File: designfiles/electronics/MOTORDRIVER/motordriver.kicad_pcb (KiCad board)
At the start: 4 copper layers, 413 parts, among them IC1 LM5109BSDX_NOPB, IC10 LM5109BSDX_NOPB, IC11 LM5109BSDX_NOPB, IC12 LM5109BSDX_NOPB, IC13 INA2181A2IDGSR, IC14 LM5109BSDX_NOPB, IC15 LM5109BSDX_NOPB, IC16 LM5109BSDX_NOPB, IC17 LM5109BSDX_NOPB, IC18 INA2181A2IDGSR, IC2 LM5109BSDX_NOPB, IC3 LM5109BSDX_NOPB, IC4 LM5109BSDX_NOPB, IC5 INA2181A2IDGSR, IC6 BQ24133RGYR, IC7 LM5176PWPR, IC8 ATSAME53J18A-MF, IC9 LM5109BSDX_NOPB, J1 IMU1, J2 IMU2, J3 Conn_01x04_Socket, J4 Screw_Terminal_01x02, J5 1-84952-1, J6 1-84952-1, J7 1-84952-1, P1 USB_C_Plug_USB2.0, Q1 30V 71A, Q10 40V 70A, Q11 30V 71A, Q12 30V 71A, Q13 30V 71A, Q14 30V 71A, Q15 30V 71A, Q16 30V 71A, Q17 30V 71A, Q18 30V 71A, Q19 30V 71A, Q2 30V 71A, Q20 30V 71A, Q21 30V 71A, Q22 30V 71A, Q23 30V 71A, Q24 30V 71A, Q25 30V 71A, Q26 30V 71A, Q27 30V 71A, Q28 30V 71A, Q3 30V 71A, Q4 30V 71A, Q5 30V 71A, Q6 30V 71A, Q7 30V 71A, Q8 30V 71A, Q9 30V 71A, SW1 SW_DPST_x2, U1 LD1117S25TR_SOT223, U2 LD1117S33TR_SOT223, U3 LD1117S50TR_SOT223, U4 TMC4671-LA, U5 ATSAMD11D14A-M, U6 TMC4671-LA, U7 TMC4671-LA

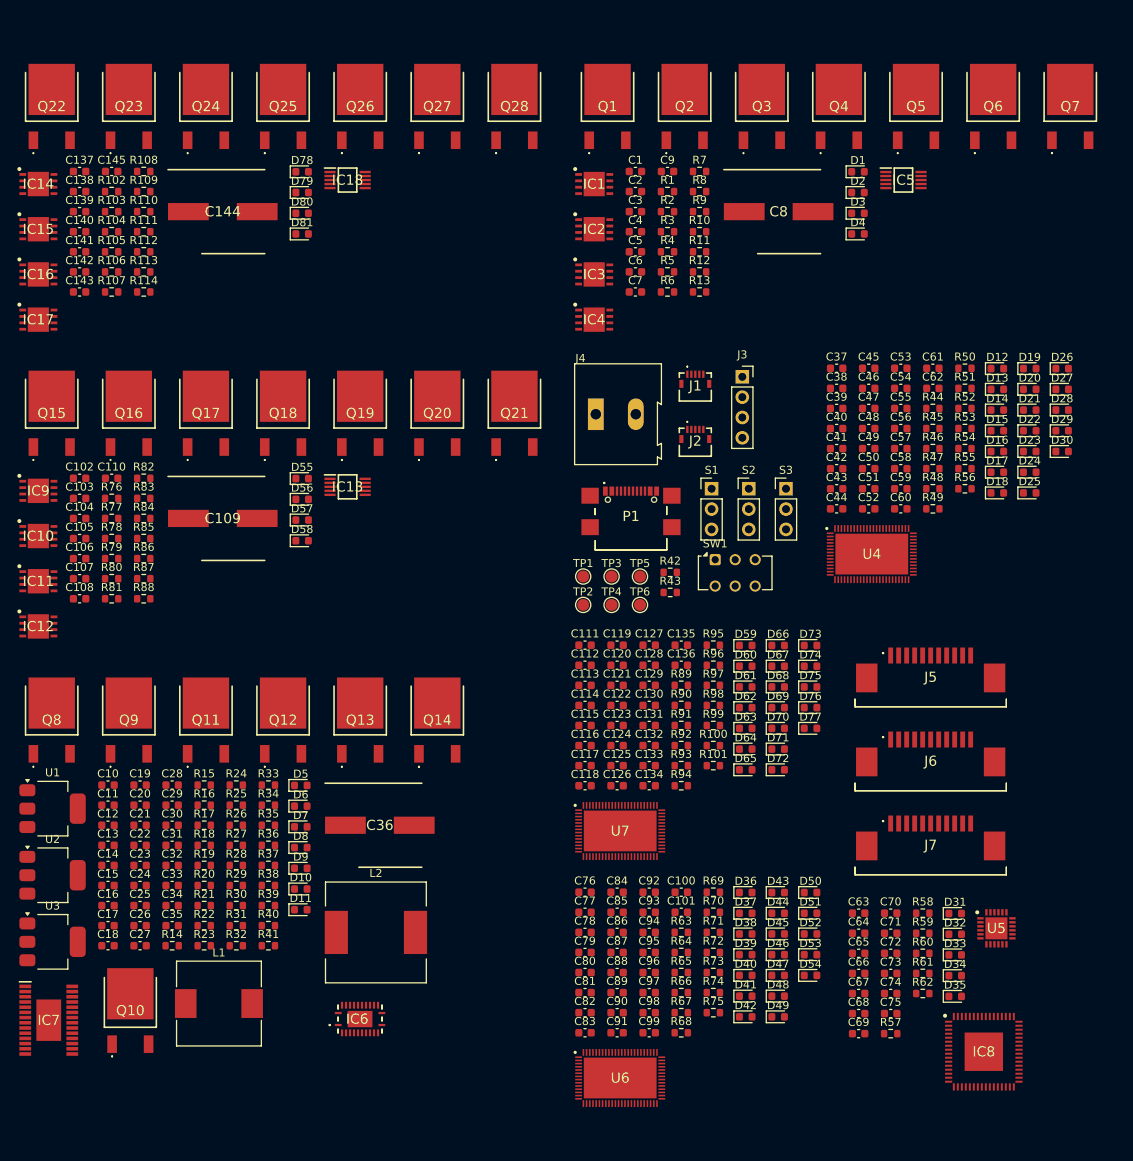
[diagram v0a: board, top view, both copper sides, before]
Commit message: removed backup files and found components for special resistors and diodes
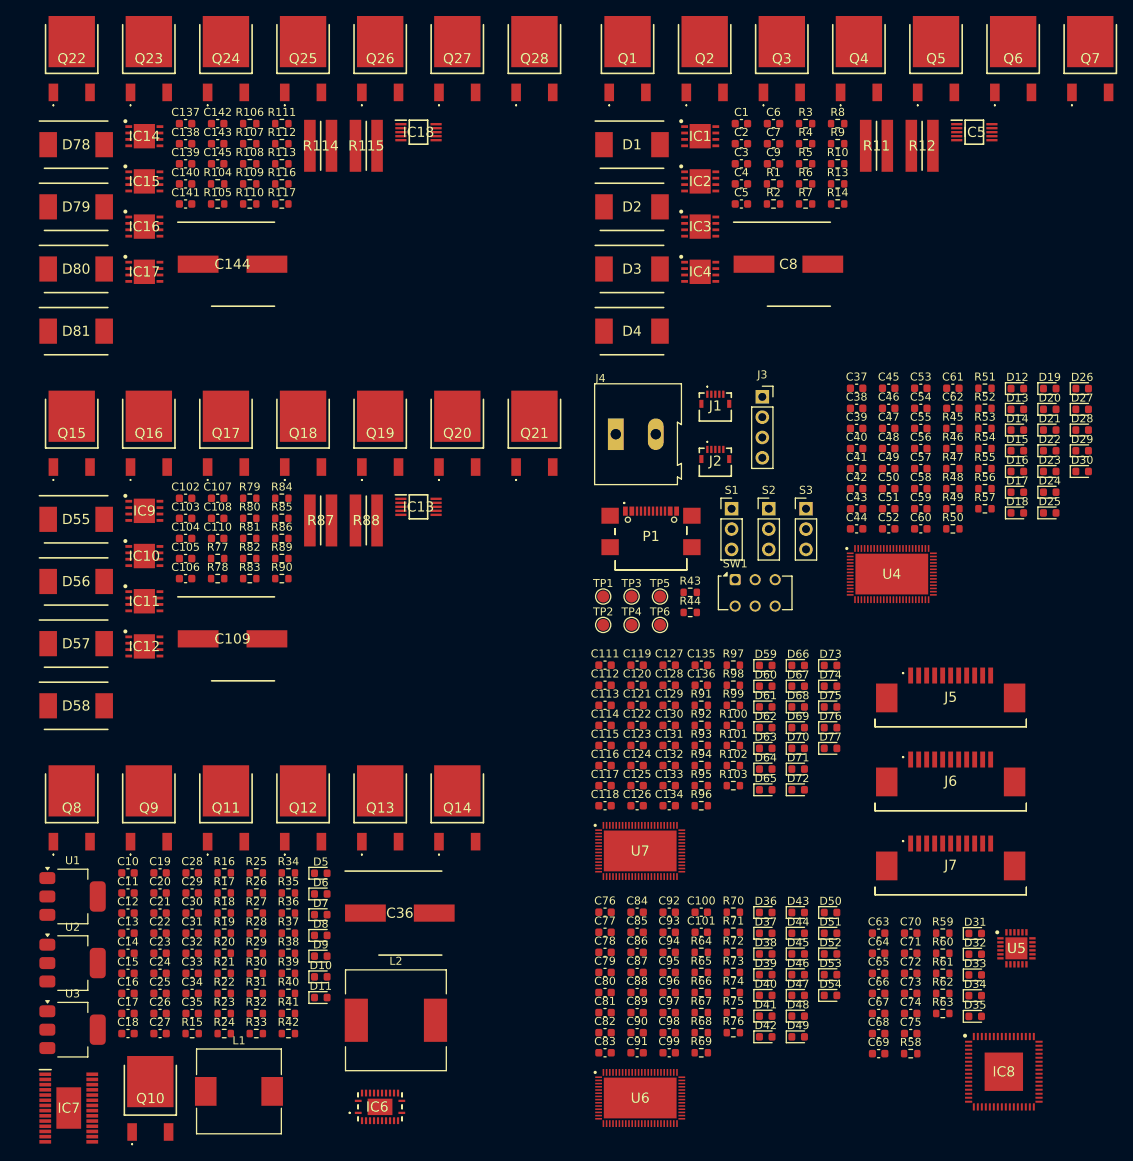
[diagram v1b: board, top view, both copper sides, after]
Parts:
- added R115: 10Ω 2W, kuben-footprints:RESC3263X80N, F.Cu at (125.9, 39.5)
- added R116: 0.01Ω, Resistor_SMD:R_0603_1608Metric, F.Cu at (115.4, 44.3)
- added R117: 0.01Ω, Resistor_SMD:R_0603_1608Metric, F.Cu at (115.4, 46.8)
- D1, D2, D3, D55, D56, D57, D78, D79, D80: value 20Vr 5A -> 4A 40V; footprint Diode_SMD:D_0603_1608Metric -> kuben-footprints:DIOM7959X262N
- D4, D58, D81: value 30Vr 5A -> 4A 40V; footprint Diode_SMD:D_0603_1608Metric -> kuben-footprints:DIOM7959X262N
- R100: value 100kΩ -> 10kΩ
- R101: value 20kΩ -> 1kΩ
- R102: value 5Ω -> 100kΩ
- R103: value 4.7Ω -> 20kΩ
- R104, R107, R110, R77, R80, R83: value 4.7Ω -> 5Ω
- R105, R108, R79, R82: value 5Ω -> 4.7Ω
- R11: value 4.7Ω 80W -> 10Ω 2W; footprint Resistor_SMD:R_0603_1608Metric -> kuben-footprints:RESC3263X80N
- R112, R86: value 4.7Ω 80W -> 4.7Ω
- R113: value 0.01Ω -> 4.7Ω
- R114, R12, R87, R88: value 0.01Ω -> 10Ω 2W; footprint Resistor_SMD:R_0603_1608Metric -> kuben-footprints:RESC3263X80N
- R14: value 10Ω -> 0.01Ω
- R15: value 2Ω -> 10Ω
- R16: value 1MΩ -> 2Ω
- R17: value 100kΩ -> 1MΩ
- R18: value 1.5kΩ -> 100kΩ
- R19: value 4.02kΩ -> 1.5kΩ
- R20: value 5.23kΩ -> 4.02kΩ
- R21: value 30.1kΩ -> 5.23kΩ
- R22: value 4.02kΩ -> 30.1kΩ
- R23: value 20mΩ -> 4.02kΩ
- R24: value 232kΩ -> 20mΩ
- R25: value 32.4kΩ -> 232kΩ
- R26: value 100kΩ -> 32.4kΩ
- R27: value 32.4kΩ -> 100kΩ
- R28: value 1kΩ -> 32.4kΩ
- R29: value 10mΩ -> 1kΩ
- R30: value 10Ω -> 10mΩ
- R31: value 1kΩ -> 10Ω
- R32: value 240kΩ -> 1kΩ
- R33: value 133kΩ -> 240kΩ
- R34: value 93.1kΩ -> 133kΩ
- R35: value 23.2kΩ -> 93.1kΩ
- R36: value 280kΩ -> 23.2kΩ
- R37: value 2kΩ -> 280kΩ
- R38: value 20kΩ -> 2kΩ
- R39: value 9.09kΩ -> 20kΩ
- R40: value 10kΩ -> 9.09kΩ
- R41: value 2mΩ -> 10kΩ
- R42: value 5.1kΩ -> 2mΩ
- R44: value 4.7kΩ -> 5.1kΩ
- R47, R66, R92, R93: value 1kΩ -> 4.7kΩ
- R50, R53, R62, R69, R72, R95, R98: value 10kΩ -> 1kΩ
- R51, R54, R70, R73, R97: value 1kΩ -> 10kΩ
- R55, R74: value 100kΩ -> 1kΩ
- R56, R75: value 20kΩ -> 100kΩ
- R57: value 1kΩ -> 20kΩ
- R63: value 4.7kΩ -> 10kΩ
- R76: value 5Ω -> 20kΩ
- R89, R90: value 4.7kΩ -> 0.01Ω
- moved R14 124.6 mm to (184.9, 46.8)
- moved R102 105.8 mm to (171.8, 117.0)
- moved R103 105.8 mm to (171.8, 119.5)
- moved R76 102.5 mm to (171.8, 150.4)
- moved R42 74.8 mm to (116.2, 150.5)
- moved R57 66.7 mm to (203.3, 84.9)
- moved R89 52.4 mm to (115.4, 91.1)
- moved R90 52.4 mm to (115.4, 93.6)
- moved R44 39.6 mm to (166.4, 97.8)
- moved D58 35.0 mm to (89.7, 109.5)
- moved R63 34.2 mm to (198.0, 148.0)
- moved D57 32.2 mm to (89.7, 101.7)
- moved R12 32.0 mm to (195.4, 39.5)
- moved R15 31.1 mm to (104.2, 150.5)
- moved R24 31.1 mm to (108.2, 150.5)
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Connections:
- R100 pad 1: +12V -> Net-(U7-NRST)
- R100 pad 2: Net-(D76-A) -> +3.3V
- R101 pad 1: Net-(D76-A) -> Net-(D75-A)
- R101 pad 2: GND -> Net-(U7-GPIO7_/_AENC_WY_MCD_/_DBGSPI_TRG)
- R102 pad 2: Net-(D78-A) -> Net-(D76-A)
- R103 pad 1: Net-(IC14-HO) -> Net-(D76-A)
- R103 pad 2: Net-(Q27-G) -> GND
- R104 pad 1: Net-(Q28-G) -> +12V
- R104 pad 2: Net-(IC14-LO) -> Net-(D78-A)
- R105 pad 1: +12V -> Net-(IC14-HO)
- R105 pad 2: Net-(D79-A) -> Net-(Q27-G)
- R106 pad 1: Net-(IC15-HO) -> Net-(Q28-G)
- R106 pad 2: Net-(Q25-G) -> Net-(IC14-LO)
- R107 pad 1: Net-(Q26-G) -> +12V
- R107 pad 2: Net-(IC15-LO) -> Net-(D79-A)
- R108 pad 1: +12V -> Net-(IC15-HO)
- R108 pad 2: Net-(D80-A) -> Net-(Q25-G)
- R109 pad 1: Net-(IC17-HO) -> Net-(Q26-G)
- R109 pad 2: Net-(Q23-G) -> Net-(IC15-LO)
- R110 pad 1: Net-(Q22-G) -> +12V
- R110 pad 2: Net-(IC16-LO) -> Net-(D80-A)
- R111 pad 1: Net-(Q24-G) -> Net-(IC17-HO)
- R111 pad 2: Net-(IC17-LO) -> Net-(Q23-G)
- R112 pad 1: +12V -> Net-(Q22-G)
- R112 pad 2: Net-(D81-A) -> Net-(IC16-LO)
- R113 pad 1: Net-(Q23-S) -> Net-(Q24-G)
- R113 pad 2: Net-(IC18-IN+1) -> Net-(IC17-LO)
- R114 pad 1: Net-(Q25-S) -> +12V
- R114 pad 2: Net-(IC18-IN+2) -> Net-(D81-A)
- R12 pad 1: Net-(Q2-S) -> +12V
- R12 pad 2: Net-(IC5-IN+1) -> Net-(D4-A)
- R13 pad 1: Net-(Q4-S) -> Net-(Q2-S)
- R13 pad 2: Net-(IC5-IN+2) -> Net-(IC5-IN+1)
- R14 pad 1: Net-(IC6-AVCC) -> Net-(Q4-S)
- R14 pad 2: Net-(D5-K) -> Net-(IC5-IN+2)
- R15 pad 1: Net-(C11-Pad1) -> Net-(IC6-AVCC)
- R15 pad 2: /IO/USBVIN -> Net-(D5-K)
- R16 pad 1: Net-(IC6-OVPSET) -> Net-(C11-Pad1)
- R17 pad 1: GND -> Net-(IC6-OVPSET)
- R17 pad 2: Net-(IC6-OVPSET) -> /IO/USBVIN
- R18 pad 1: /voltageregulators/IC5_VREF -> GND
- R18 pad 2: Net-(D7-A) -> Net-(IC6-OVPSET)
- R19 pad 1: Net-(IC6-ACDRV) -> /voltageregulators/IC5_VREF
- R19 pad 2: Net-(Q8-G) -> Net-(D7-A)
- R20 pad 1: Net-(IC6-TS) -> Net-(IC6-ACDRV)
- R20 pad 2: /voltageregulators/IC5_VREF -> Net-(Q8-G)
- R21 pad 1: GND -> Net-(IC6-TS)
- R21 pad 2: Net-(IC6-TS) -> /voltageregulators/IC5_VREF
- R22 pad 1: Net-(IC6-CMSRC) -> GND
- R22 pad 2: Net-(IC6-ACP) -> Net-(IC6-TS)
- R23 pad 1: Net-(D8-A) -> Net-(IC6-CMSRC)
- R24 pad 1: Net-(IC6-ISET) -> Net-(D8-A)
- R24 pad 2: /voltageregulators/IC5_VREF -> Net-(IC6-ACP)
- R25 pad 2: GND -> /voltageregulators/IC5_VREF
- R26 pad 1: Net-(IC6-ACSET) -> Net-(IC6-ISET)
- R26 pad 2: /voltageregulators/IC5_VREF -> GND
- R27 pad 1: GND -> Net-(IC6-ACSET)
- R27 pad 2: Net-(IC6-ACSET) -> /voltageregulators/IC5_VREF
- R28 pad 1: Net-(Q10-G) -> GND
- R28 pad 2: Net-(IC6-~{BATDRV}) -> Net-(IC6-ACSET)
- R29 pad 1: /IO/BATTVIN -> Net-(Q10-G)
- R29 pad 2: Net-(IC6-SRP) -> Net-(IC6-~{BATDRV})
- R30 pad 1: Net-(IC7-VIN) -> /IO/BATTVIN
- R30 pad 2: Net-(D8-K) -> Net-(IC6-SRP)
- R31 pad 1: Net-(D9-A) -> Net-(IC7-VIN)
- R31 pad 2: +3.3V -> Net-(D8-K)
- R32 pad 1: Net-(IC7-EN/UVLO) -> Net-(D9-A)
- R32 pad 2: Net-(D8-A) -> +3.3V
- R33 pad 1: GND -> Net-(IC7-EN/UVLO)
- R33 pad 2: Net-(IC7-EN/UVLO) -> Net-(D8-A)
- R34 pad 2: Net-(IC7-MODE) -> Net-(IC7-EN/UVLO)
- R35 pad 2: Net-(IC7-RT) -> Net-(IC7-MODE)
- R36 pad 1: Net-(IC7-FB) -> GND
- R36 pad 2: +12V -> Net-(IC7-RT)
- R37 pad 1: Net-(IC7-VISNS) -> Net-(IC7-FB)
- R37 pad 2: Net-(D8-A) -> +12V
- R38 pad 1: GND -> Net-(IC7-VISNS)
- R38 pad 2: Net-(IC7-FB) -> Net-(D8-A)
- R39 pad 1: Net-(C30-Pad2) -> GND
- R39 pad 2: Net-(IC7-COMP) -> Net-(IC7-FB)
- R40 pad 1: Net-(D10-A) -> Net-(C30-Pad2)
- R40 pad 2: Net-(IC7-PGOOD) -> Net-(IC7-COMP)
- R41 pad 1: GND -> Net-(D10-A)
- R41 pad 2: Net-(IC7-CSG) -> Net-(IC7-PGOOD)
- R42 pad 1: Net-(P1-PadA5) -> GND
- R42 pad 2: GND -> Net-(IC7-CSG)
- R43 pad 1: GND -> Net-(P1-PadA5)
- R43 pad 2: Net-(P1-PadB5) -> GND
- R44 pad 1: +5V -> GND
- R44 pad 2: /driverIC/HALL_U -> Net-(P1-PadB5)
- R45 pad 2: /driverIC/HALL_V -> /driverIC/HALL_U
- R46 pad 2: /driverIC/HALL_W -> /driverIC/HALL_V
- R47 pad 1: /driverIC/HALL_W -> +5V
- R48 pad 1: /driverIC/HALL_V -> /driverIC/HALL_W
- R48 pad 2: /driverIC/HALL_V -> /driverIC/HALL_W
- R49 pad 1: /driverIC/HALL_U -> /driverIC/HALL_V
- R49 pad 2: /driverIC/HALL_U -> /driverIC/HALL_V
- R50 pad 1: /driverIC/ENI -> /driverIC/HALL_U
- R50 pad 2: GND -> /driverIC/HALL_U
- R51 pad 1: Net-(D26-A) -> /driverIC/ENI
- R51 pad 2: Net-(U4-GPIO5_/_AENC_UX_MCD_/_DBGSPI_MOSI) -> GND
- R52 pad 1: Net-(D27-A) -> Net-(D26-A)
- R52 pad 2: Net-(U4-GPIO6_/_AENC_VN_MCD_/_DBGSPI_MISO) -> Net-(U4-GPIO5_/_AENC_UX_MCD_/_DBGSPI_MOSI)
- R53 pad 1: Net-(U4-NRST) -> Net-(D27-A)
- R53 pad 2: +3.3V -> Net-(U4-GPIO6_/_AENC_VN_MCD_/_DBGSPI_MISO)
- R54 pad 1: Net-(D28-A) -> Net-(U4-NRST)
- R54 pad 2: Net-(U4-GPIO7_/_AENC_WY_MCD_/_DBGSPI_TRG) -> +3.3V
- R55 pad 1: +12V -> Net-(D28-A)
- R55 pad 2: Net-(D29-A) -> Net-(U4-GPIO7_/_AENC_WY_MCD_/_DBGSPI_TRG)
- R56 pad 1: Net-(D29-A) -> +12V
- R56 pad 2: GND -> Net-(D29-A)
- R57 pad 1: Net-(D31-A) -> Net-(D29-A)
- R57 pad 2: /microcontrollers/ERRLED -> GND
- R58 pad 1: Net-(D32-A) -> Net-(D31-A)
- R58 pad 2: /microcontrollers/PROCLED -> /microcontrollers/ERRLED
- R59 pad 1: Net-(D33-A) -> Net-(D32-A)
- R59 pad 2: /microcontrollers/STATUS1 -> /microcontrollers/PROCLED
- R60 pad 1: Net-(D34-A) -> Net-(D33-A)
- R60 pad 2: /microcontrollers/STATUS2 -> /microcontrollers/STATUS1
- R61 pad 1: Net-(D35-A) -> Net-(D34-A)
- R61 pad 2: /microcontrollers/STATUS3 -> /microcontrollers/STATUS2
- R62 pad 1: Net-(U5-PA28/~{RESET}) -> Net-(D35-A)
- R62 pad 2: +3.3V -> /microcontrollers/STATUS3
- R63 pad 1: +5V -> Net-(U5-PA28/~{RESET})
- R63 pad 2: /driverIC1/HALL_U -> +3.3V
- R64 pad 2: /driverIC1/HALL_V -> /driverIC1/HALL_U
- R65 pad 2: /driverIC1/HALL_W -> /driverIC1/HALL_V
- R66 pad 1: /driverIC1/HALL_W -> +5V
- R67 pad 1: /driverIC1/HALL_V -> /driverIC1/HALL_W
- R67 pad 2: /driverIC1/HALL_V -> /driverIC1/HALL_W
- R68 pad 1: /driverIC1/HALL_U -> /driverIC1/HALL_V
- R68 pad 2: /driverIC1/HALL_U -> /driverIC1/HALL_V
- R69 pad 1: /driverIC1/ENI -> /driverIC1/HALL_U
- R69 pad 2: GND -> /driverIC1/HALL_U
- R70 pad 1: Net-(D50-A) -> /driverIC1/ENI
- R70 pad 2: Net-(U6-GPIO5_/_AENC_UX_MCD_/_DBGSPI_MOSI) -> GND
- R71 pad 1: Net-(D51-A) -> Net-(D50-A)
- R71 pad 2: Net-(U6-GPIO6_/_AENC_VN_MCD_/_DBGSPI_MISO) -> Net-(U6-GPIO5_/_AENC_UX_MCD_/_DBGSPI_MOSI)
- R72 pad 1: Net-(U6-NRST) -> Net-(D51-A)
- R72 pad 2: +3.3V -> Net-(U6-GPIO6_/_AENC_VN_MCD_/_DBGSPI_MISO)
- R73 pad 1: Net-(D52-A) -> Net-(U6-NRST)
- R73 pad 2: Net-(U6-GPIO7_/_AENC_WY_MCD_/_DBGSPI_TRG) -> +3.3V
- R74 pad 1: +12V -> Net-(D52-A)
- R74 pad 2: Net-(D53-A) -> Net-(U6-GPIO7_/_AENC_WY_MCD_/_DBGSPI_TRG)
- R75 pad 1: Net-(D53-A) -> +12V
- R75 pad 2: GND -> Net-(D53-A)
- R76 pad 1: +12V -> Net-(D53-A)
- R76 pad 2: Net-(D55-A) -> GND
- R77 pad 1: Net-(IC9-HO) -> +12V
- R77 pad 2: Net-(Q20-G) -> Net-(D55-A)
- R78 pad 1: Net-(Q21-G) -> Net-(IC9-HO)
- R78 pad 2: Net-(IC9-LO) -> Net-(Q20-G)
- R79 pad 1: +12V -> Net-(Q21-G)
- R79 pad 2: Net-(D56-A) -> Net-(IC9-LO)
- R80 pad 1: Net-(IC10-HO) -> +12V
- R80 pad 2: Net-(Q18-G) -> Net-(D56-A)
- R81 pad 1: Net-(Q19-G) -> Net-(IC10-HO)
- R81 pad 2: Net-(IC10-LO) -> Net-(Q18-G)
- R82 pad 1: +12V -> Net-(Q19-G)
- R82 pad 2: Net-(D57-A) -> Net-(IC10-LO)
- R83 pad 1: Net-(IC12-HO) -> +12V
- R83 pad 2: Net-(Q16-G) -> Net-(D57-A)
- R84 pad 1: Net-(Q15-G) -> Net-(IC12-HO)
- R84 pad 2: Net-(IC11-LO) -> Net-(Q16-G)
- R85 pad 1: Net-(Q17-G) -> Net-(Q15-G)
- R85 pad 2: Net-(IC12-LO) -> Net-(IC11-LO)
- R86 pad 1: +12V -> Net-(Q17-G)
- R86 pad 2: Net-(D58-A) -> Net-(IC12-LO)
- R87 pad 1: Net-(Q16-S) -> +12V
- R87 pad 2: Net-(IC13-IN+1) -> Net-(D58-A)
- R88 pad 1: Net-(Q18-S) -> +12V
- R88 pad 2: Net-(IC13-IN+2) -> Net-(D58-A)
- R89 pad 1: +5V -> Net-(Q16-S)
- R89 pad 2: /driverIC2/HALL_U -> Net-(IC13-IN+1)
- R90 pad 1: +5V -> Net-(Q18-S)
- R90 pad 2: /driverIC2/HALL_V -> Net-(IC13-IN+2)
- R91 pad 2: /driverIC2/HALL_W -> /driverIC2/HALL_U
- R92 pad 1: /driverIC2/HALL_W -> +5V
- R92 pad 2: /driverIC2/HALL_W -> /driverIC2/HALL_V
- R93 pad 1: /driverIC2/HALL_V -> +5V
- R93 pad 2: /driverIC2/HALL_V -> /driverIC2/HALL_W
- R94 pad 1: /driverIC2/HALL_U -> /driverIC2/HALL_W
- R94 pad 2: /driverIC2/HALL_U -> /driverIC2/HALL_W
- R95 pad 1: /driverIC2/ENI -> /driverIC2/HALL_V
- R95 pad 2: GND -> /driverIC2/HALL_V
- R96 pad 1: Net-(D73-A) -> /driverIC2/HALL_U
- R96 pad 2: Net-(U7-GPIO5_/_AENC_UX_MCD_/_DBGSPI_MOSI) -> /driverIC2/HALL_U
- R97 pad 1: Net-(D74-A) -> /driverIC2/ENI
- R97 pad 2: Net-(U7-GPIO6_/_AENC_VN_MCD_/_DBGSPI_MISO) -> GND
- R98 pad 1: Net-(U7-NRST) -> Net-(D73-A)
- R98 pad 2: +3.3V -> Net-(U7-GPIO5_/_AENC_UX_MCD_/_DBGSPI_MOSI)
- R99 pad 1: Net-(D75-A) -> Net-(D74-A)
- R99 pad 2: Net-(U7-GPIO7_/_AENC_WY_MCD_/_DBGSPI_TRG) -> Net-(U7-GPIO6_/_AENC_VN_MCD_/_DBGSPI_MISO)

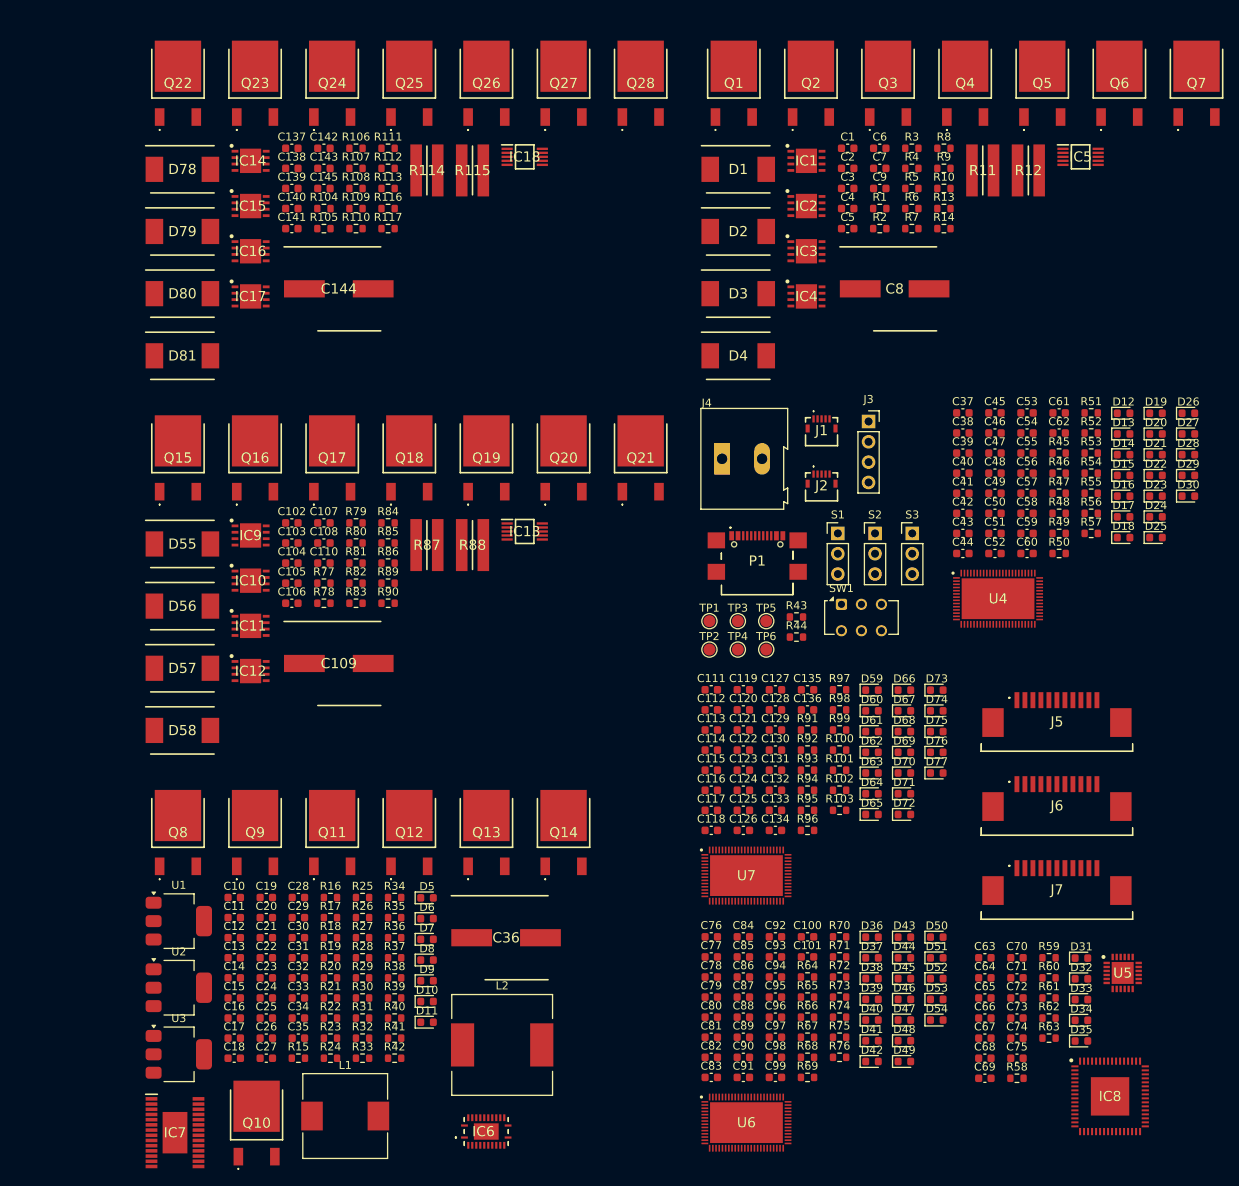
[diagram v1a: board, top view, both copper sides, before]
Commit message: added diodes
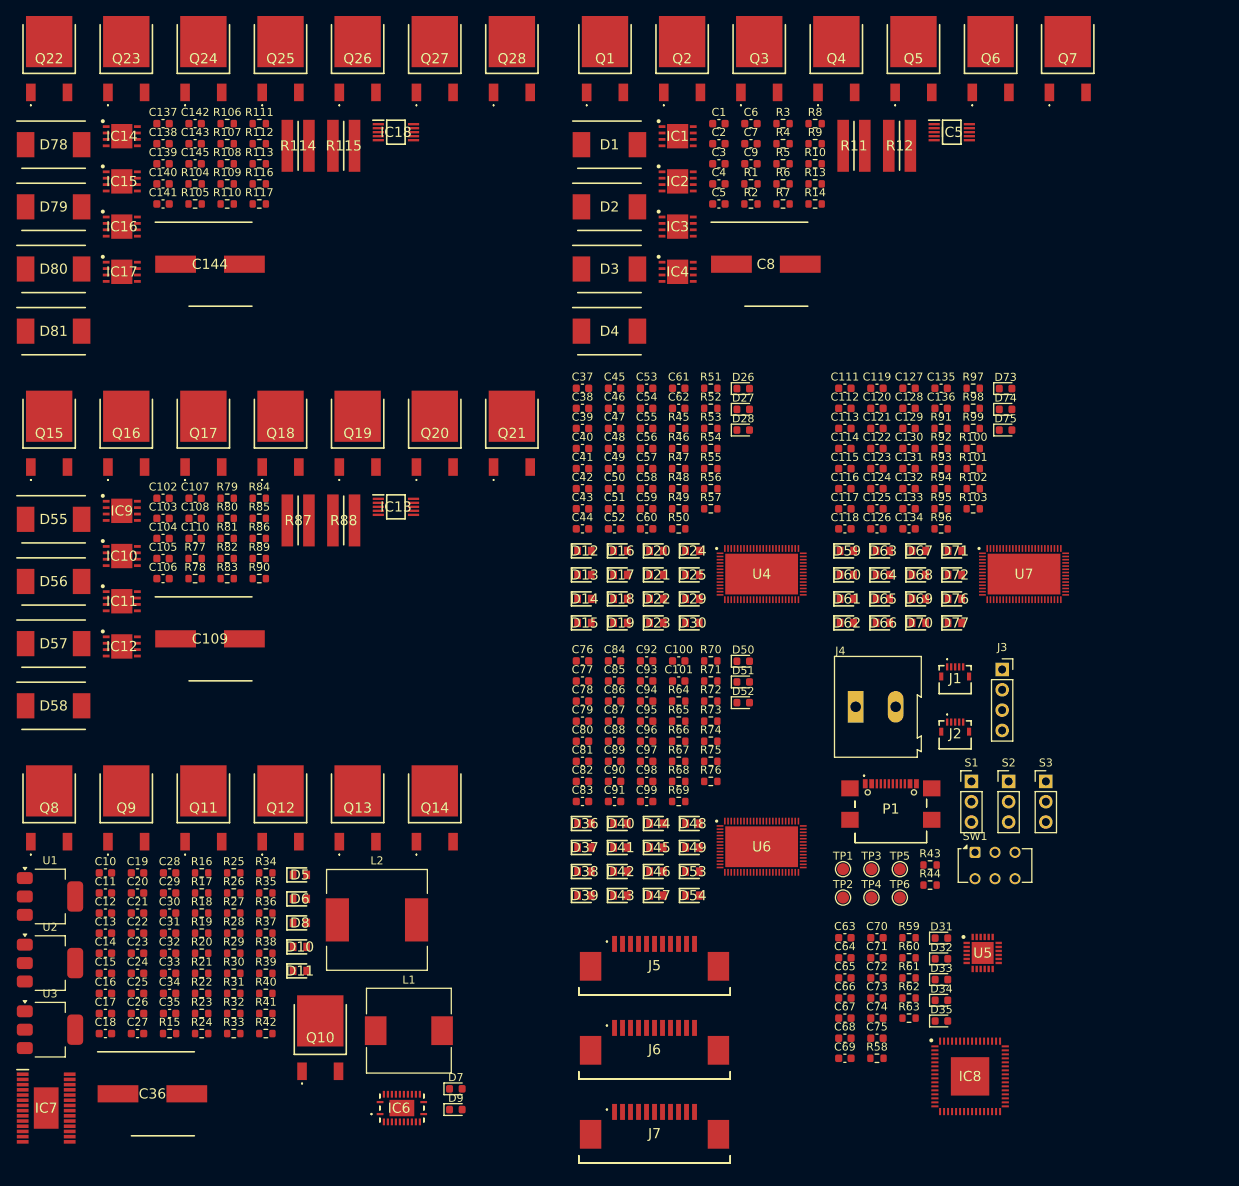
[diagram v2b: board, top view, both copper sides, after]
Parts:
- D10: value 385mVf 500mA -> 4.7Vf 0.5A; footprint Diode_SMD:D_0603_1608Metric -> kuben-footprints:DIOC1709X85N
- D11, D12, D13, D16, D17, D20, D21, D22, D23, D24, D25, D29, D30, D36, D37, D40, D41, D44, D45, D46, D47, D48, D49, D5, D53, D54, D59, D6, D60, D63, D64, D67, D68, D69, D70, D71, D72, D76, D77, D8: value 470mVf 500mA -> 4.7Vf 0.5A; footprint Diode_SMD:D_0603_1608Metric -> kuben-footprints:DIOC1709X85N
- D14, D15, D18, D19, D38, D39, D42, D43, D61, D62, D65, D66: value 470mV 500mA -> 4.7Vf 0.5A; footprint Diode_SMD:D_0603_1608Metric -> kuben-footprints:DIOC1709X85N
- moved D19 71.9 mm to (144.4, 96.1)
- moved D15 69.9 mm to (139.9, 96.1)
- moved D14 69.8 mm to (139.9, 93.1)
- moved D13 69.7 mm to (139.9, 90.1)
- moved D12 69.6 mm to (139.9, 87.1)
- moved D23 64.4 mm to (148.9, 96.1)
- moved D22 64.3 mm to (148.9, 93.1)
- moved D21 64.2 mm to (148.9, 90.1)
- moved D20 64.1 mm to (148.9, 87.1)
- moved D30 64.0 mm to (153.4, 96.1)
- moved D29 63.9 mm to (153.4, 93.1)
- moved D18 63.4 mm to (144.4, 93.1)
- moved D17 63.3 mm to (144.4, 90.1)
- moved D16 63.3 mm to (144.4, 87.1)
- moved J5 58.8 mm to (148.7, 139.9)
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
